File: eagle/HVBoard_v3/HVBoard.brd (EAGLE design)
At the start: 176.5 x 64.8 mm, 47 parts, among them IC1 LM555N, K1 TX2-12V, K2 TX2-12V, Q1 IRF510, Q2 IRF510, Q3 IRF9530, Q4 IRF9540, Q5 IRF9540

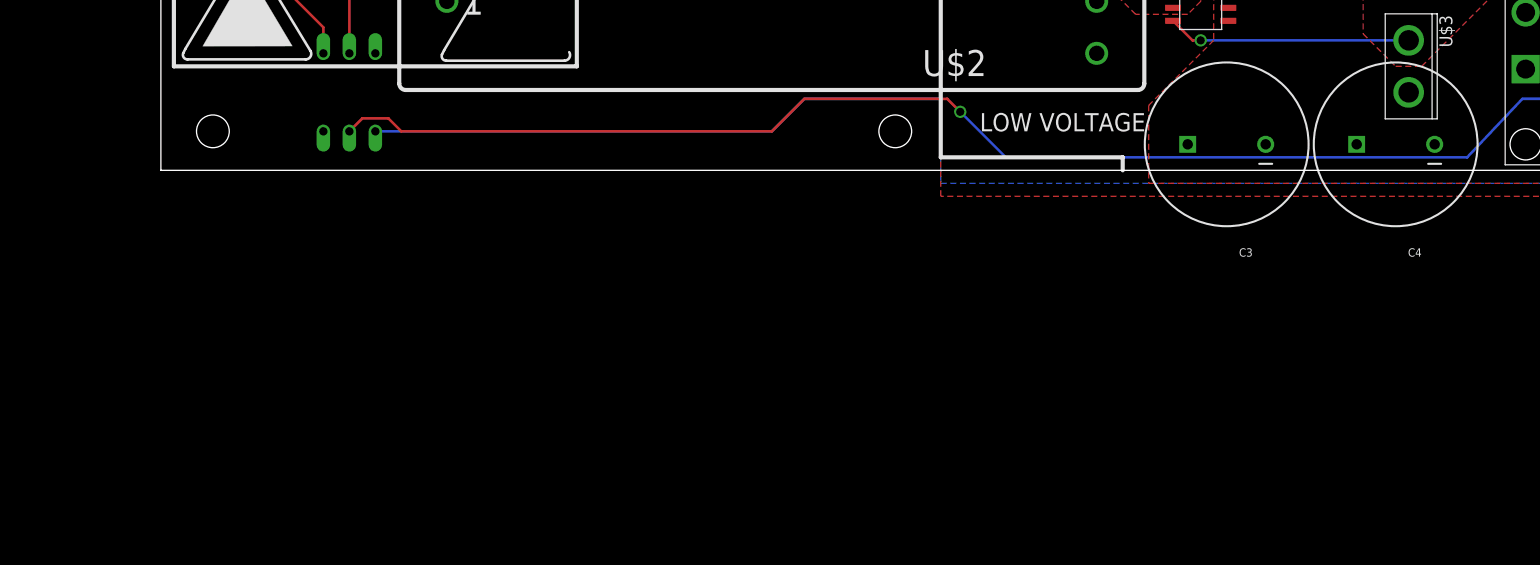
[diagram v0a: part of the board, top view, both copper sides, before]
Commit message: added some EAGLE
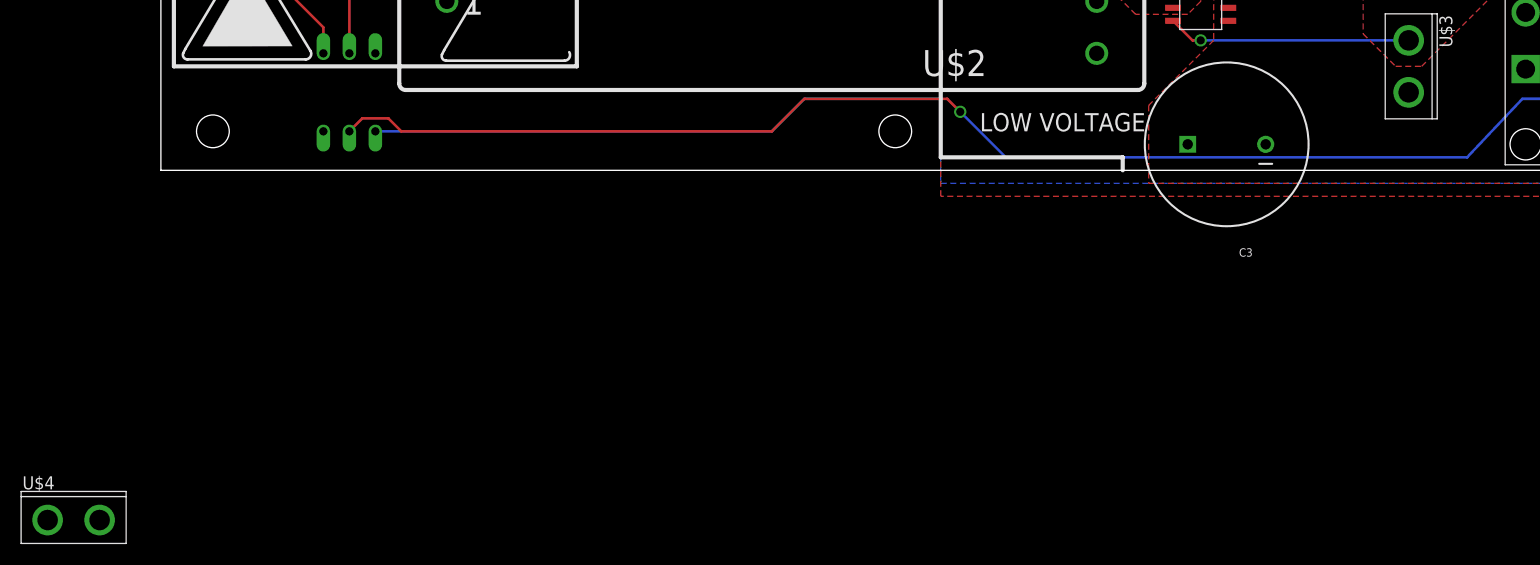
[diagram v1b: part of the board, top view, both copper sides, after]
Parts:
- removed C4: 4700uF, SparkFun-Capacitors:CPOL-RADIAL-1000UF-63V
- added U$4: VFT2045BP-M3/4W, MHR15-GLV_PWR:VFT2045BP-M3/4W
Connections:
- new net N$7: U$1.P5, U$1.P6, U$1.P7, U$1.P8, U$4.P1
- net GND: no longer C4.2
- net PSL: now also U$4.P2; no longer C4.1, U$1.P5, U$1.P6, U$1.P7, U$1.P8
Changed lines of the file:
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@@
 <element name="R2" library="resistor" package="R0603" value="10k" x="145.415" y="49.53" rot="R180"/>
 <element name="C3" library="SparkFun-Capacitors" package="CPOL-RADIAL-1000UF-63V" value="4700uF" x="104.14" y="33.02" rot="R180"/>
-<element name="C4" library="SparkFun-Capacitors" package="CPOL-RADIAL-1000UF-63V" value="4700uF" x="120.65" y="33.02" rot="R180"/>
 <element name="U$2" library="MHR15-TS" package="110IMY70-15-0TZG" value="110IMY70-15-0TZG" x="59.69" y="62.23" rot="R180"/>
 <element name="R5" library="rcl" package="R0805" value="" x="97.79" y="81.28" rot="R90"/>
@@
 <element name="GND_CON" library="mhybrid molex megaFit" package="2PIN_MOLEXMINIFIT" value="MINIFIT_2PIN" x="149.86" y="33.02"/>
 <element name="Q5" library="transistor-power" package="TO220BV" value="IRF9540" x="9.525" y="56.515"/>
+<element name="U$4" library="MHR15-GLV_PWR" package="VFT2045BP-M3/4W" value="VFT2045BP-M3/4W" x="-8.52805" y="-3.68935">
+<attribute name="MFC_PN" value="VFT2045BP-M3/4W" x="-8.52805" y="-3.68935" size="1.778" layer="27" display="off"/>
+<attribute name="MANUFACTURER" value="Vishay Semiconductor Diodes Division" x="-8.52805" y="-3.68935" size="1.778" layer="27" display="off"/>
+<attribute name="DIGIKEY_PN" value="VFT2045BP-M3/4W-ND" x="-8.52805" y="-3.68935" size="1.778" layer="27" display="off"/>
+</element>
 </elements>
 <signals>
@@
 <contactref element="K1" pad="12"/>
 <contactref element="R2" pad="1"/>
-<contactref element="C4" pad="2"/>
 <contactref element="C3" pad="2"/>
 <contactref element="U$2" pad="P14"/>
@@
 <wire x1="62.865" y1="37.465" x2="59.69" y2="34.29" width="0.254" layer="16"/>
 <wire x1="59.69" y1="34.29" x2="20.955" y2="34.29" width="0.254" layer="16"/>
+<wire x1="142.875" y1="88.9" x2="147.32" y2="86.36" width="0" layer="19" extent="1-1"/>
+<wire x1="143.51" y1="77.47" x2="147.32" y2="86.36" width="0" layer="19" extent="1-1"/>
+<wire x1="127" y1="82.55" x2="133.0325" y2="77.78" width="0" layer="19" extent="1-1"/>
+<wire x1="127" y1="86.36" x2="127" y2="82.55" width="0" layer="19" extent="1-1"/>
+<wire x1="143.51" y1="68.58" x2="143.51" y2="77.47" width="0" layer="19" extent="1-1"/>
+<wire x1="149.86" y1="69.85" x2="143.51" y2="68.58" width="0" layer="19" extent="1-1"/>
+<wire x1="118.96" y1="70.1" x2="127" y2="82.55" width="0" layer="19" extent="1-1"/>
+<wire x1="112.56" y1="65.7" x2="118.96" y2="70.1" width="0" layer="19" extent="1-1"/>
+<wire x1="106.26" y1="65.7" x2="112.56" y2="65.7" width="0" layer="19" extent="1-1"/>
+<wire x1="102.16" y1="65.7" x2="106.26" y2="65.7" width="0" layer="19" extent="1-1"/>
+<wire x1="106.26" y1="70.1" x2="106.26" y2="65.7" width="0" layer="19" extent="1-1"/>
+<wire x1="102.16" y1="61.3" x2="102.16" y2="65.7" width="0" layer="19" extent="1-1"/>
+<wire x1="102.16" y1="56.9" x2="102.16" y2="61.3" width="0" layer="19" extent="1-1"/>
+<wire x1="113.03" y1="75.565" x2="118.96" y2="70.1" width="0" layer="19" extent="1-1"/>
+<wire x1="107.95" y1="81.28" x2="113.03" y2="75.565" width="0" layer="19" extent="1-1"/>
+<wire x1="97.79" y1="80.33" x2="107.95" y2="81.28" width="0" layer="19" extent="1-1"/>
+<wire x1="91.44" y1="57.15" x2="102.16" y2="56.9" width="0" layer="19" extent="1-1"/>
+<wire x1="91.44" y1="62.23" x2="91.44" y2="57.15" width="0" layer="19" extent="1-1"/>
+<wire x1="111.76" y1="91.44" x2="107.95" y2="81.28" width="0" layer="19" extent="1-1"/>
+<wire x1="149.86" y1="53.34" x2="143.51" y2="68.58" width="0" layer="19" extent="1-1"/>
+<wire x1="149.86" y1="45.91" x2="146.265" y2="49.53" width="0" layer="19" extent="1-1"/>
+<wire x1="149.86" y1="40.37" x2="149.86" y2="45.91" width="0" layer="19" extent="1-1"/>
+<wire x1="161.1" y1="38.1" x2="149.86" y2="40.37" width="0" layer="19" extent="1-1"/>
+<wire x1="161.1" y1="33.655" x2="161.1" y2="38.1" width="0" layer="19" extent="1-1"/>
+<wire x1="161.1" y1="43.18" x2="161.1" y2="38.1" width="0" layer="19" extent="1-1"/>
+<wire x1="107.95" y1="33.02" x2="102.16" y2="56.9" width="0" layer="19" extent="1-1"/>
+<wire x1="76.2" y1="37.465" x2="91.44" y2="57.15" width="0" layer="19" extent="16-16"/>
 </signal>
 <signal name="N$6">
@@
 </signal>
 <signal name="PSL">
-<contactref element="U$1" pad="P5"/>
-<contactref element="U$1" pad="P6"/>
-<contactref element="U$1" pad="P7"/>
-<contactref element="U$1" pad="P8"/>
 <contactref element="U$3" pad="P2"/>
 <contactref element="C3" pad="1"/>
-<contactref element="C4" pad="1"/>
 <contactref element="PRE_SAFETY_12V" pad="P$2"/>
 <polygon width="0.254" layer="1" rank="4">
@@
 <vertex x="132.715" y="49.53"/>
 </polygon>
+<contactref element="U$4" pad="P2"/>
+<wire x1="121.92" y1="38.1" x2="133.35" y2="45.91" width="0" layer="19" extent="1-1"/>
+<wire x1="100.33" y1="33.02" x2="121.92" y2="38.1" width="0" layer="19" extent="1-1"/>
+<wire x1="-5.98805" y1="-3.68935" x2="100.33" y2="33.02" width="0" layer="19" extent="1-1"/>
 </signal>
 <signal name="N$5">
@@
 <wire x1="143.256" y1="86.36" x2="142.875" y2="86.36" width="0.254" layer="16"/>
 </signal>
+<signal name="N$7">
+<contactref element="U$1" pad="P5"/>
+<contactref element="U$1" pad="P6"/>
+<contactref element="U$1" pad="P7"/>
+<contactref element="U$1" pad="P8"/>
+<contactref element="U$4" pad="P1"/>
+<wire x1="104.3" y1="47.625" x2="104.3" y2="48.895" width="0" layer="19" extent="1-1"/>
+<wire x1="104.3" y1="46.355" x2="104.3" y2="47.625" width="0" layer="19" extent="1-1"/>
+<wire x1="104.3" y1="45.085" x2="104.3" y2="46.355" width="0" layer="19" extent="1-1"/>
+<wire x1="-11.06805" y1="-3.68935" x2="104.3" y2="45.085" width="0" layer="19" extent="1-1"/>
+</signal>
 </signals>
